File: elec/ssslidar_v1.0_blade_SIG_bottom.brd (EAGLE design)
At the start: 12 x 10.5 mm, 31 parts, among them P1 PIN_SMD_0.8X1_RECT, P10 PIN_SMD_1X2, P11 PIN_SMD_1X2, P12 PIN_SMD_1X2, P13 PIN_SMD_1X2, P14 PIN_SMD_0.8X1_RECT, P15 PIN_SMD_0.8X1_RECT, P16 PIN_SMD_1X2, P17 PIN_SMD_1X2, P18 PIN_SMD_0.8X1_RECT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

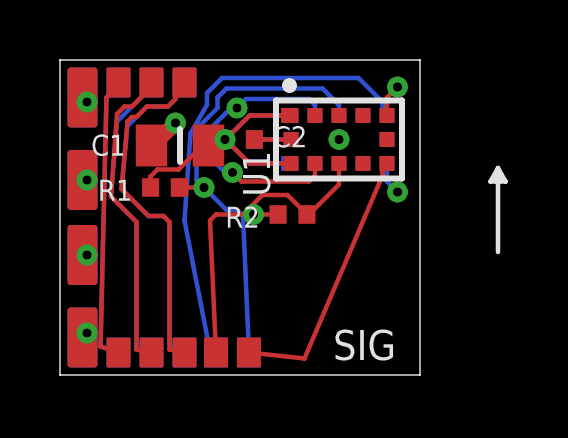
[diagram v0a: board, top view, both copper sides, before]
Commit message: Blades redesign done.
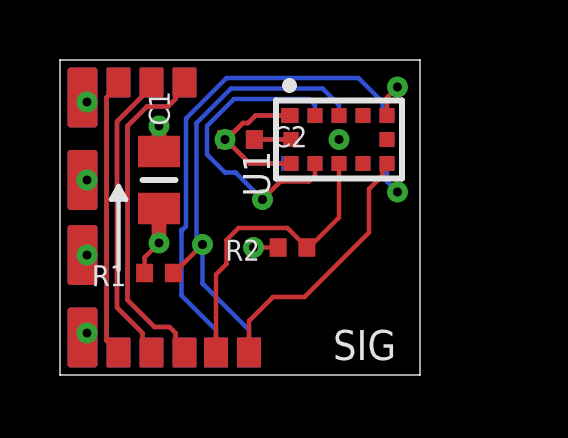
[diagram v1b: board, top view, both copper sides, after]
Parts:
- moved R1 2.86 mm to (3.30, 3.40)
- moved C1 1.35 mm to (3.30, 6.50), turned to 90 degrees
- moved R2 1.10 mm to (7.75, 4.25)
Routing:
- net VDD: track 16.7 -> 15.7 mm, vias 5 -> 6
- net SCL: vias 3 -> 2

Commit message: Updated all libs.
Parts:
- turned P10 to 90 degrees
- turned P11 to 90 degrees
- turned P12 to 90 degrees
- turned P13 to 270 degrees
- turned P16 to 270 degrees
- turned P17 to 270 degrees
- turned P2 to 270 degrees
- turned P9 to 90 degrees
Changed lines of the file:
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@@
 <element name="U1" library="VL53L0X" package="VL53L0X" value="VL53L0X" x="9.3" y="7.85" rot="R90"/>
 <element name="U2" library="VL53L0X" package="VL53L0X" value="VL53L0X" x="9.3" y="7.85" rot="MR270"/>
-<element name="P2" library="Xevelabs" package="PIN_SMD_1X2" value="PIN_SMD_1X2" x="0.75" y="9.25" rot="MR0"/>
+<element name="P2" library="Xevelabs" package="PIN_SMD_1X2" value="PIN_SMD_1X2" x="0.75" y="9.25" rot="MR270"/>
 <element name="P4" library="Xevelabs" package="PIN_SMD_0.8X1_RECT" value="PIN_SMD_0.8X1_RECT" x="5.2" y="0.75" rot="R90"/>
 <element name="P5" library="Xevelabs" package="PIN_SMD_0.8X1_RECT" value="PIN_SMD_0.8X1_RECT" x="6.3" y="0.75" rot="MR90"/>
 <element name="P6" library="Xevelabs" package="PIN_SMD_0.8X1_RECT" value="PIN_SMD_0.8X1_RECT" x="6.3" y="0.75" rot="R90"/>
 <element name="P7" library="Xevelabs" package="PIN_SMD_0.8X1_RECT" value="PIN_SMD_0.8X1_RECT" x="5.2" y="0.75" rot="MR90"/>
-<element name="P16" library="Xevelabs" package="PIN_SMD_1X2" value="PIN_SMD_1X2" x="0.75" y="4" rot="R180"/>
-<element name="P17" library="Xevelabs" package="PIN_SMD_1X2" value="PIN_SMD_1X2" x="0.75" y="1.25" rot="MR0"/>
-<element name="P9" library="Xevelabs" package="PIN_SMD_1X2" value="PIN_SMD_1X2" x="0.75" y="9.25"/>
-<element name="P10" library="Xevelabs" package="PIN_SMD_1X2" value="PIN_SMD_1X2" x="0.75" y="6.5" rot="MR180"/>
-<element name="P11" library="Xevelabs" package="PIN_SMD_1X2" value="PIN_SMD_1X2" x="0.75" y="1.25"/>
-<element name="P12" library="Xevelabs" package="PIN_SMD_1X2" value="PIN_SMD_1X2" x="0.75" y="6.5"/>
-<element name="P13" library="Xevelabs" package="PIN_SMD_1X2" value="PIN_SMD_1X2" x="0.75" y="4" rot="MR0"/>
+<element name="P16" library="Xevelabs" package="PIN_SMD_1X2" value="PIN_SMD_1X2" x="0.75" y="4" rot="R270"/>
+<element name="P17" library="Xevelabs" package="PIN_SMD_1X2" value="PIN_SMD_1X2" x="0.75" y="1.25" rot="MR270"/>
+<element name="P9" library="Xevelabs" package="PIN_SMD_1X2" value="PIN_SMD_1X2" x="0.75" y="9.25" rot="R90"/>
+<element name="P10" library="Xevelabs" package="PIN_SMD_1X2" value="PIN_SMD_1X2" x="0.75" y="6.5" rot="MR90"/>
+<element name="P11" library="Xevelabs" package="PIN_SMD_1X2" value="PIN_SMD_1X2" x="0.75" y="1.25" rot="R90"/>
+<element name="P12" library="Xevelabs" package="PIN_SMD_1X2" value="PIN_SMD_1X2" x="0.75" y="6.5" rot="R90"/>
+<element name="P13" library="Xevelabs" package="PIN_SMD_1X2" value="PIN_SMD_1X2" x="0.75" y="4" rot="MR270"/>
 <element name="P14" library="Xevelabs" package="PIN_SMD_0.8X1_RECT" value="PIN_SMD_0.8X1_RECT" x="1.95" y="9.75" rot="R90"/>
 <element name="P15" library="Xevelabs" package="PIN_SMD_0.8X1_RECT" value="PIN_SMD_0.8X1_RECT" x="3.05" y="0.75" rot="R90"/>
